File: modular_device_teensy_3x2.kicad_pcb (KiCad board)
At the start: 2 copper layers, 83.8 x 40.6 mm, 23 parts, among them P1 PWR_JACK_2.5x5.5_SMD_RA, P2 HEADER_01X03_SMD_RA, P3 HEADER_01X03_SMD_RA, P4 HEADER_01X03_SMD_RA, P5 BNC_DOUBLE_RA, P6 HEADER_01X02_SMD_RA, P7 HEADER_01X02_SMD_RA, SW1 KT_SWITCH

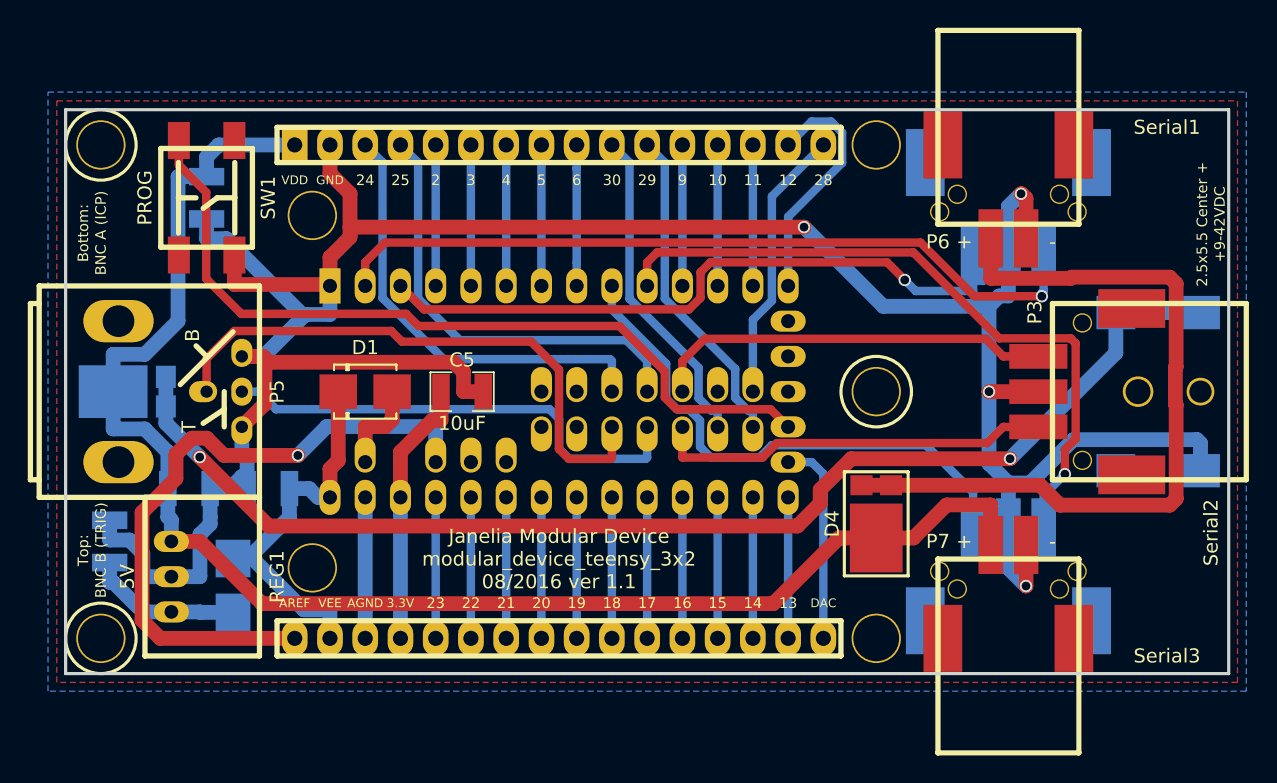
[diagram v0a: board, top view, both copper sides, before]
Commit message: Silkscreen modifications.
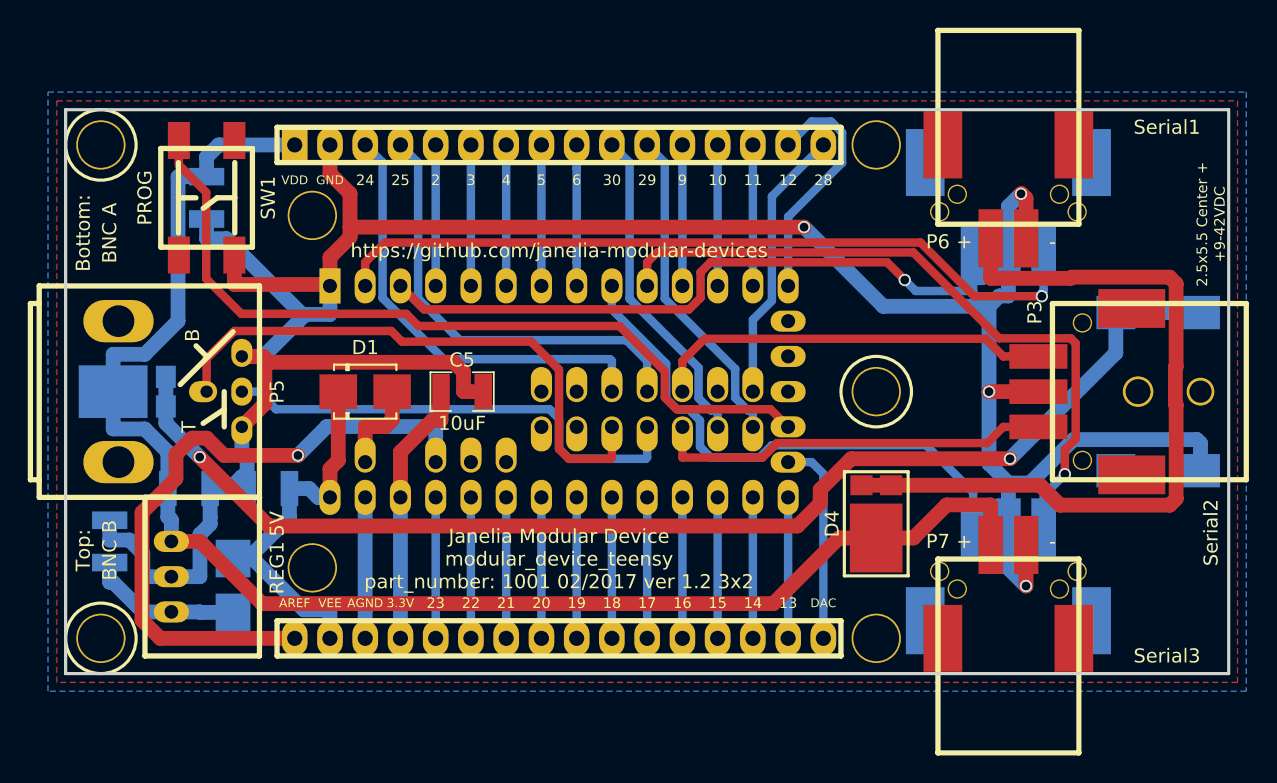
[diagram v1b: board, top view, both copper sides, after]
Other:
- board text added: "Janelia Modular Device modular_device_teensy part_number: 1001 02/2017 ver 1.2 3x2"
- board text added: "https://github.com/janelia-modular-devices"
- board text removed: "Janelia Modular Device modular_device_teensy_3x2 08/2016 ver 1.1"
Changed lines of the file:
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@@
-(kicad_pcb (version 4) (host pcbnew 4.1.0-alpha+201608010716+6997~46~ubuntu16.04.1-product)
+(kicad_pcb (version 20170123) (host pcbnew no-vcs-found-7571~57~ubuntu16.04.1)
   (general
     (links 73)
@@
     (area 56.090457 73.215499 149.140334 126.174501)
     (thickness 1.6)
-    (drawings 23)
+    (drawings 25)
     (tracks 327)
     (zones 0)
@@
   (title_block
     (title modular_device_teensy_3x2)
-    (rev 1.1)
+    (rev 1.2)
   )
   (layers
-    (0 F.Cu signal hide)
+    (0 F.Cu signal)
     (31 B.Cu signal)
     (32 B.Adhes user)
@@
     (add_net /TX3)
   )
+  (module modular_device_teensy_3x2:DO-214BA (layer B.Cu)
+    (at 71.755 113.665 270)
+    (descr "Microsemi LSM115J")
+    (tags "DO-214BA diode")
+    (attr smd)
+    (fp_text reference D2 (at 4.445 0 180) (layer B.SilkS)
+      (effects (font (size 1.016 1.016) (thickness 0.254)) (justify mirror))
+    )
+    (fp_text value diode_schottky_15V_1A (at 0 -3 270) (layer B.SilkS) hide
+      (effects (font (size 1 1) (thickness 0.15)) (justify mirror))
+    )
+    (fp_line (start 2.25 -1.95) (end -2.25 -1.95) (layer B.SilkS) (width 0.15))
+    (fp_line (start -2.25 1.95) (end 2.25 1.95) (layer B.SilkS) (width 0.15))
+    (fp_line (start -1.2 1.55) (end -1.2 1.95) (layer B.SilkS) (width 0.15))
+    (fp_line (start -1.35 1.55) (end -1.2 1.55) (layer B.SilkS) (width 0.15))
+    (fp_line (start -1.35 1.95) (end -1.35 1.55) (layer B.SilkS) (width 0.15))
+    (fp_line (start -1.2 -1.55) (end -1.2 -1.95) (layer B.SilkS) (width 0.15))
+    (fp_line (start -1.35 -1.55) (end -1.2 -1.55) (layer B.SilkS) (width 0.15))
+    (fp_line (start -1.35 -1.95) (end -1.35 -1.55) (layer B.SilkS) (width 0.15))
+    (fp_line (start 2.25 1.95) (end 2.25 1.55) (layer B.SilkS) (width 0.15))
+    (fp_line (start 2.25 -1.95) (end 2.25 -1.55) (layer B.SilkS) (width 0.15))
+    (fp_line (start -2.25 -1.95) (end -2.25 -1.55) (layer B.SilkS) (width 0.15))
+    (fp_line (start -2.25 1.95) (end -2.25 1.55) (layer B.SilkS) (width 0.15))
+    (fp_line (start -3 -2.25) (end -3 2.25) (layer B.CrtYd) (width 0.05))
+    (fp_line (start 3 -2.25) (end -3 -2.25) (layer B.CrtYd) (width 0.05))
+    (fp_line (start 3 2.25) (end 3 -2.25) (layer B.CrtYd) (width 0.05))
+    (fp_line (start -3 2.25) (end 3 2.25) (layer B.CrtYd) (width 0.05))
+    (pad 1 smd rect (at -1.94 0 270) (size 2.71 2.5) (layers B.Cu B.Paste B.Mask)
+      (net 11 VEE))
+    (pad 2 smd rect (at 1.94 0 270) (size 2.71 2.5) (layers B.Cu B.Paste B.Mask)
+      (net 7 +5V))
+  )
   (module modular_device_teensy_3x2:SM1210 (layer B.Cu)
     (at 68.58 106.68)
@@
   (module modular_device_teensy_3x2:DC_DC_CONV_R78C (layer F.Cu)
     (at 67.31 113.03 270)
-    (fp_text reference REG1 (at 0 -7.62 270) (layer F.SilkS)
+    (fp_text reference REG1 (at -0.635 -7.62 270) (layer F.SilkS)
       (effects (font (size 1.016 1.016) (thickness 0.254)))
     )
@@
       (effects (font (size 1.016 1.016) (thickness 0.254)))
     )
-    (fp_text user "BNC B (TRIG)" (at -11.43 -1.27 90) (layer F.SilkS)
-      (effects (font (size 0.762 0.762) (thickness 0.1905)))
-    )
-    (fp_text user "BNC A (ICP)" (at 11.43 -1.27 270) (layer F.SilkS)
-      (effects (font (size 0.762 0.762) (thickness 0.1905)))
+    (fp_text user "BNC B" (at -11.43 -0.635 90) (layer F.SilkS)
+      (effects (font (size 1.016 1.016) (thickness 0.254)))
+    )
+    (fp_text user "BNC A" (at 11.43 -0.635 90) (layer F.SilkS)
+      (effects (font (size 1.016 1.016) (thickness 0.254)))
     )
     (fp_line (start 2.54 6.35) (end 3.302 5.588) (layer F.SilkS) (width 0.381))
@@
       (net 11 VEE))
   )
-  (module modular_device_teensy_3x2:DO-214BA (layer B.Cu)
-    (at 71.755 113.665 270)
-    (descr "Microsemi LSM115J")
-    (tags "DO-214BA diode")
-    (attr smd)
-    (fp_text reference D2 (at 4.445 0 540) (layer B.SilkS)
-      (effects (font (size 1.016 1.016) (thickness 0.254)) (justify mirror))
-    )
-    (fp_text value diode_schottky_15V_1A (at 0 -3 270) (layer B.SilkS) hide
-      (effects (font (size 1 1) (thickness 0.15)) (justify mirror))
-    )
-    (fp_line (start -3 2.25) (end 3 2.25) (layer B.CrtYd) (width 0.05))
-    (fp_line (start 3 2.25) (end 3 -2.25) (layer B.CrtYd) (width 0.05))
-    (fp_line (start 3 -2.25) (end -3 -2.25) (layer B.CrtYd) (width 0.05))
-    (fp_line (start -3 -2.25) (end -3 2.25) (layer B.CrtYd) (width 0.05))
-    (fp_line (start -2.25 1.95) (end -2.25 1.55) (layer B.SilkS) (width 0.15))
-    (fp_line (start -2.25 -1.95) (end -2.25 -1.55) (layer B.SilkS) (width 0.15))
-    (fp_line (start 2.25 -1.95) (end 2.25 -1.55) (layer B.SilkS) (width 0.15))
-    (fp_line (start 2.25 1.95) (end 2.25 1.55) (layer B.SilkS) (width 0.15))
-    (fp_line (start -1.35 -1.95) (end -1.35 -1.55) (layer B.SilkS) (width 0.15))
-    (fp_line (start -1.35 -1.55) (end -1.2 -1.55) (layer B.SilkS) (width 0.15))
-    (fp_line (start -1.2 -1.55) (end -1.2 -1.95) (layer B.SilkS) (width 0.15))
-    (fp_line (start -1.35 1.95) (end -1.35 1.55) (layer B.SilkS) (width 0.15))
-    (fp_line (start -1.35 1.55) (end -1.2 1.55) (layer B.SilkS) (width 0.15))
-    (fp_line (start -1.2 1.55) (end -1.2 1.95) (layer B.SilkS) (width 0.15))
-    (fp_line (start -2.25 1.95) (end 2.25 1.95) (layer B.SilkS) (width 0.15))
-    (fp_line (start 2.25 -1.95) (end -2.25 -1.95) (layer B.SilkS) (width 0.15))
-    (pad 2 smd rect (at 1.94 0 270) (size 2.71 2.5) (layers B.Cu B.Paste B.Mask)
-      (net 7 +5V))
-    (pad 1 smd rect (at -1.94 0 270) (size 2.71 2.5) (layers B.Cu B.Paste B.Mask)
-      (net 11 VEE))
-  )
   (module modular_device_teensy_3x2:MOUNTING_HOLE_4-40 (layer F.Cu)
     (at 62.23 81.915)
@@
     (pad "" thru_hole circle (at 22.86 -17.78) (size 3.556 3.556) (drill 3.302) (layers *.Cu *.Mask F.SilkS))
   )
+  (gr_text https://github.com/janelia-modular-devices (at 95.25 89.535) (layer B.SilkS)
+    (effects (font (size 1.016 1.016) (thickness 0.254)) (justify mirror))
+  )
+  (gr_text https://github.com/janelia-modular-devices (at 95.25 89.535) (layer F.SilkS)
+    (effects (font (size 1.016 1.016) (thickness 0.254)))
+  )
   (gr_line (start 143.51 79.375) (end 59.69 79.375) (angle 90) (layer Edge.Cuts) (width 0.2286))
   (gr_line (start 143.51 120.015) (end 143.51 79.375) (angle 90) (layer Edge.Cuts) (width 0.2286))
   (gr_line (start 59.69 120.015) (end 143.51 120.015) (angle 90) (layer Edge.Cuts) (width 0.2286))
   (gr_text Top: (at 60.96 111.125 90) (layer F.SilkS)
-    (effects (font (size 0.762 0.762) (thickness 0.1905)))
+    (effects (font (size 1.016 1.016) (thickness 0.254)))
   )
   (gr_text Bottom: (at 60.96 88.265 90) (layer F.SilkS)
-    (effects (font (size 0.762 0.762) (thickness 0.1905)))
-  )
-  (gr_text "Janelia Modular Device\nmodular_device_teensy_3x2\n08/2016 ver 1.1" (at 95.25 111.76) (layer B.SilkS)
+    (effects (font (size 1.016 1.016) (thickness 0.254)))
+  )
+  (gr_text "Janelia Modular Device\nmodular_device_teensy\npart_number: 1001 02/2017 ver 1.2 3x2" (at 95.25 111.76) (layer B.SilkS)
     (effects (font (size 1.016 1.016) (thickness 0.254)) (justify mirror))
   )
@@
     (effects (font (size 1.016 1.016) (thickness 0.254)) (justify mirror))
   )
-  (gr_text 5V (at 64.135 113.03 90) (layer F.SilkS)
+  (gr_text 5V (at 74.93 109.22 90) (layer F.SilkS)
     (effects (font (size 1.016 1.016) (thickness 0.254)))
   )
-  (gr_text "Janelia Modular Device\nmodular_device_teensy_3x2\n08/2016 ver 1.1" (at 95.25 111.76) (layer F.SilkS)
+  (gr_text "Janelia Modular Device\nmodular_device_teensy\npart_number: 1001 02/2017 ver 1.2 3x2" (at 95.25 111.76) (layer F.SilkS)
     (effects (font (size 1.016 1.016) (thickness 0.254)))
   )
